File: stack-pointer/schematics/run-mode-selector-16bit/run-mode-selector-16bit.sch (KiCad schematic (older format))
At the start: 17 parts, among them SW1 SW_DIP_x08, SW2 SW_DIP_x08, SW3 SW_SPDT, U1 74LS157, U2 74LS157, U3 74LS157, U4 74LS157

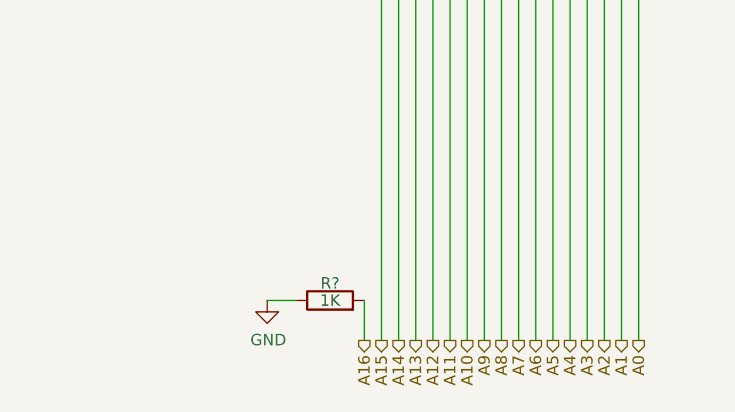
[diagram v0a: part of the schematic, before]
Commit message: added schematics to documentation
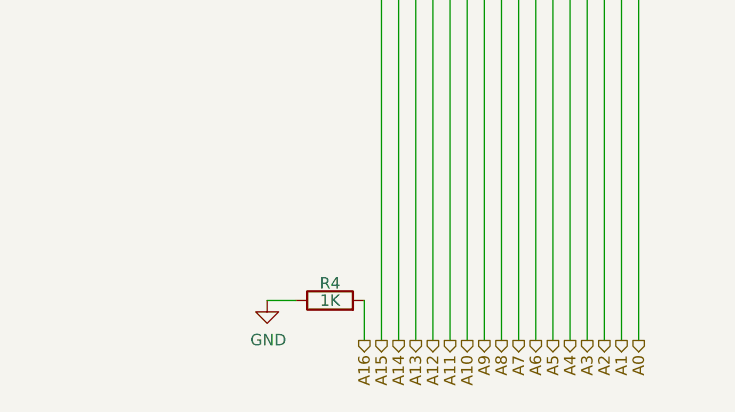
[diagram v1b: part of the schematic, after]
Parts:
- gave numbers to parts that had none: 1
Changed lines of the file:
@@
 A16
 $Comp
-L power:GND #PWR?
+L power:GND #PWR09
 U 1 1 6105A225
 P 1650 7325
-F 0 "#PWR?" H 1650 7075 50  0001 C CNN
+F 0 "#PWR09" H 1650 7075 50  0001 C CNN
 F 1 "GND" H 1655 7152 50  0000 C CNN
 F 2 "" H 1650 7325 50  0001 C CNN
@@
 $EndComp
 $Comp
-L Device:R R?
+L Device:R R4
 U 1 1 6105B7B2
 P 1925 7325
-F 0 "R?" V 2000 7325 50  0000 C CNN
+F 0 "R4" V 2000 7325 50  0000 C CNN
 F 1 "1K" V 1925 7325 50  0000 C CNN
 F 2 "" V 1855 7325 50  0001 C CNN
